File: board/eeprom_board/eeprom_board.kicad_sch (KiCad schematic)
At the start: 6 parts, among them J1 Conn_01x04_Pin, U1 AT24C02C-SSHM-T, U2 AT24C32D-SSHM-T

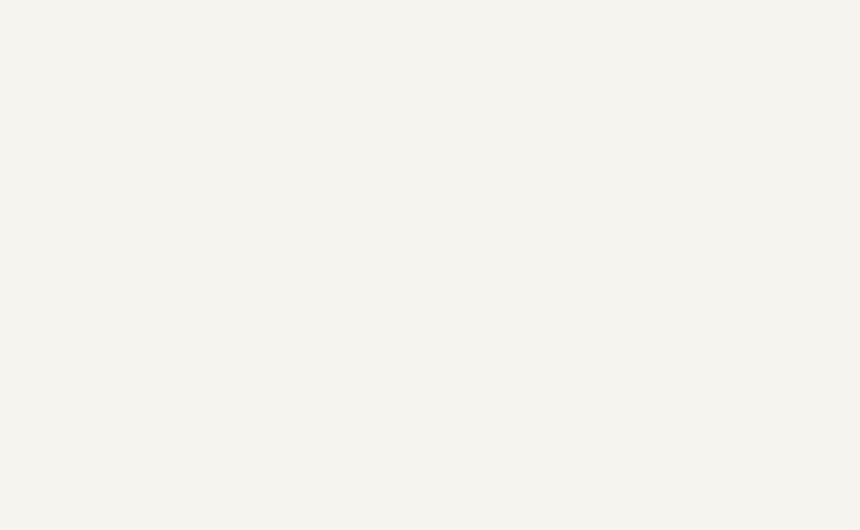
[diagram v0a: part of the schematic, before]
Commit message: Check ACK from device
Check the acks received from device to test i2c device presence.
No ack no device present.
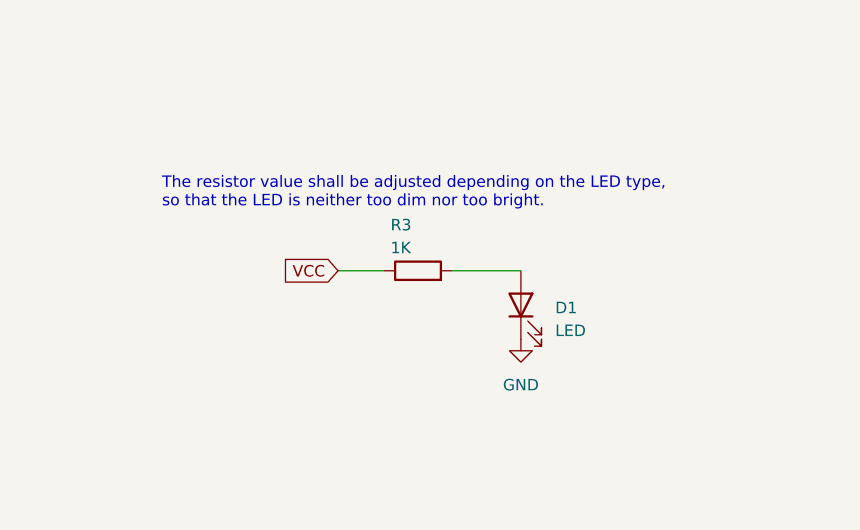
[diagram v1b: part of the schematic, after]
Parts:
- added D1: LED, LED_SMD:LED_0603_1608Metric_Pad1.05x0.95mm_HandSolder, symbol Device:LED
- added R3: 1K, Resistor_SMD:R_0603_1608Metric_Pad0.98x0.95mm_HandSolder, symbol Device:R
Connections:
- net GND: now also D1.1 (K)
- net VCC: now also R3.1
- new net: D1.2 (A), R3.2
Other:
- note added: "The resistor value shall be adjusted depending on the LED type, so that the LED is neither too dim nor too bright."
